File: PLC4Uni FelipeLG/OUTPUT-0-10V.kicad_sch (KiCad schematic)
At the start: 6 parts

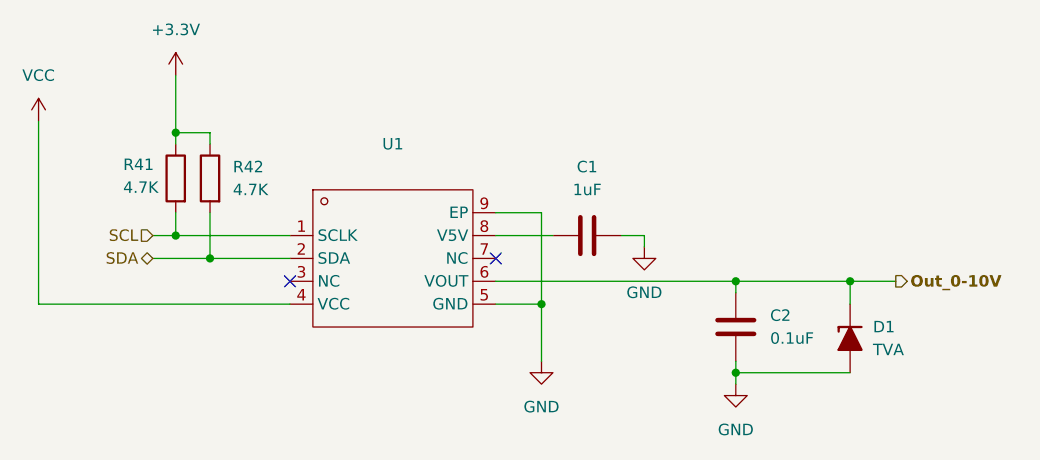
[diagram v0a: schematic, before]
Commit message: Add files via upload
Updated Circuitos corregidos y pistas agregadas
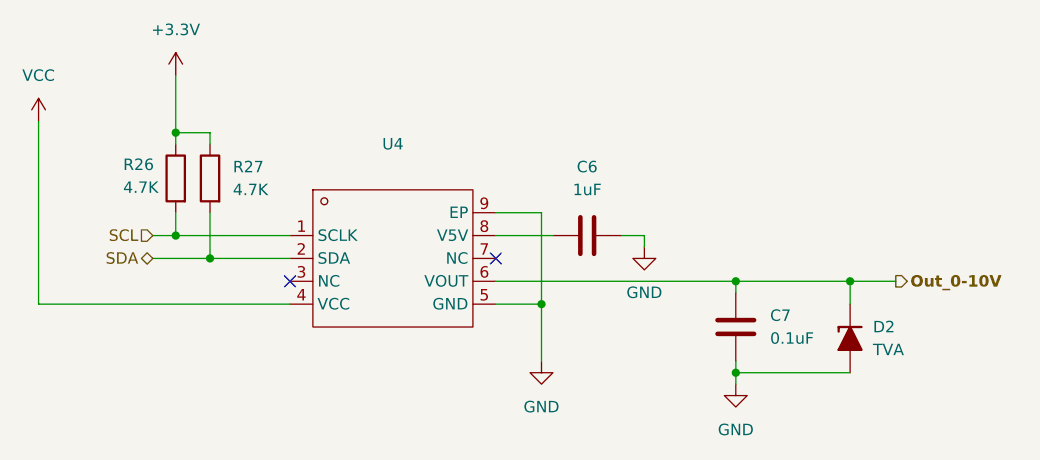
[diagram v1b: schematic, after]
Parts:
- renumbered C1 to C6, C2 to C7, D1 to D2, R41 to R26, R42 to R27, U1 to U4
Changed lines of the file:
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@@
 		(dnp no)
 		(fields_autoplaced yes)
-		(property "Reference" "#PWR053"
+		(property "Reference" "#PWR054"
 			(at 158.75 120.65 0)
 			(effects
@@
 			(project "Diseños de circuitos"
 				(path "/65c875c0-73bd-43df-b6cd-4a685398cace/3b453a73-5bb7-4645-a7e8-6e186968fa05/cb3f1452-6c69-43d9-8153-9dbf3dca2d0d"
-					(reference "#PWR053")
+					(reference "#PWR054")
 					(unit 1)
 				)
@@
 		(dnp no)
 		(fields_autoplaced yes)
-		(property "Reference" "C1"
+		(property "Reference" "C6"
 			(at 163.83 92.71 90)
 			(effects
@@
 			(project "Diseños de circuitos"
 				(path "/65c875c0-73bd-43df-b6cd-4a685398cace/3b453a73-5bb7-4645-a7e8-6e186968fa05/cb3f1452-6c69-43d9-8153-9dbf3dca2d0d"
-					(reference "C1")
+					(reference "C6")
 					(unit 1)
 				)
@@
 		(dnp no)
 		(fields_autoplaced yes)
-		(property "Reference" "R42"
+		(property "Reference" "R27"
 			(at 124.46 92.7099 0)
 			(effects
@@
 			(project "Diseños de circuitos"
 				(path "/65c875c0-73bd-43df-b6cd-4a685398cace/3b453a73-5bb7-4645-a7e8-6e186968fa05/cb3f1452-6c69-43d9-8153-9dbf3dca2d0d"
-					(reference "R42")
+					(reference "R27")
 					(unit 1)
 				)
@@
 		(dnp no)
 		(fields_autoplaced yes)
-		(property "Reference" "U1"
+		(property "Reference" "U4"
 			(at 142.24 90.17 0)
 			(effects
@@
 			(project "Diseños de circuitos"
 				(path "/65c875c0-73bd-43df-b6cd-4a685398cace/3b453a73-5bb7-4645-a7e8-6e186968fa05/cb3f1452-6c69-43d9-8153-9dbf3dca2d0d"
-					(reference "U1")
+					(reference "U4")
 					(unit 1)
 				)
@@
 		(dnp no)
 		(fields_autoplaced yes)
-		(property "Reference" "#PWR052"
+		(property "Reference" "#PWR053"
 			(at 118.11 86.36 0)
 			(effects
@@
 			(project "Diseños de circuitos"
 				(path "/65c875c0-73bd-43df-b6cd-4a685398cace/3b453a73-5bb7-4645-a7e8-6e186968fa05/cb3f1452-6c69-43d9-8153-9dbf3dca2d0d"
-					(reference "#PWR052")
+					(reference "#PWR053")
 					(unit 1)
 				)
@@
 		(dnp no)
 		(fields_autoplaced yes)
-		(property "Reference" "#PWR054"
+		(property "Reference" "#PWR055"
 			(at 170.18 107.95 0)
 			(effects
@@
 			(project "Diseños de circuitos"
 				(path "/65c875c0-73bd-43df-b6cd-4a685398cace/3b453a73-5bb7-4645-a7e8-6e186968fa05/cb3f1452-6c69-43d9-8153-9dbf3dca2d0d"
-					(reference "#PWR054")
+					(reference "#PWR055")
 					(unit 1)
 				)
@@
 		(dnp no)
 		(fields_autoplaced yes)
-		(property "Reference" "C2"
+		(property "Reference" "C7"
 			(at 184.15 109.2199 0)
 			(effects
@@
 			(project "Diseños de circuitos"
 				(path "/65c875c0-73bd-43df-b6cd-4a685398cace/3b453a73-5bb7-4645-a7e8-6e186968fa05/cb3f1452-6c69-43d9-8153-9dbf3dca2d0d"
-					(reference "C2")
+					(reference "C7")
 					(unit 1)
 				)
@@
 		(on_board yes)
 		(dnp no)
-		(property "Reference" "R41"
+		(property "Reference" "R26"
 			(at 112.268 92.456 0)
 			(effects
@@
 			(project "Diseños de circuitos"
 				(path "/65c875c0-73bd-43df-b6cd-4a685398cace/3b453a73-5bb7-4645-a7e8-6e186968fa05/cb3f1452-6c69-43d9-8153-9dbf3dca2d0d"
-					(reference "R41")
+					(reference "R26")
 					(unit 1)
 				)
@@
 		(dnp no)
 		(fields_autoplaced yes)
-		(property "Reference" "D1"
+		(property "Reference" "D2"
 			(at 195.58 110.4899 90)
 			(effects
@@
 			(project "Diseños de circuitos"
 				(path "/65c875c0-73bd-43df-b6cd-4a685398cace/3b453a73-5bb7-4645-a7e8-6e186968fa05/cb3f1452-6c69-43d9-8153-9dbf3dca2d0d"
-					(reference "D1")
+					(reference "D2")
 					(unit 1)
 				)
@@
 		(dnp no)
 		(fields_autoplaced yes)
-		(property "Reference" "#PWR056"
+		(property "Reference" "#PWR052"
 			(at 102.87 91.44 0)
 			(effects
@@
 			(project ""
 				(path "/65c875c0-73bd-43df-b6cd-4a685398cace/3b453a73-5bb7-4645-a7e8-6e186968fa05/cb3f1452-6c69-43d9-8153-9dbf3dca2d0d"
-					(reference "#PWR056")
+					(reference "#PWR052")
 					(unit 1)
 				)
@@
 		(dnp no)
 		(fields_autoplaced yes)
-		(property "Reference" "#PWR055"
+		(property "Reference" "#PWR056"
 			(at 180.34 123.19 0)
 			(effects
@@
 			(project "Diseños de circuitos"
 				(path "/65c875c0-73bd-43df-b6cd-4a685398cace/3b453a73-5bb7-4645-a7e8-6e186968fa05/cb3f1452-6c69-43d9-8153-9dbf3dca2d0d"
-					(reference "#PWR055")
-					(unit 1)
-				)
+					(reference "#PWR056")
+					(unit 1)
+				)
